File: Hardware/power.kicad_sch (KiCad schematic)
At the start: 42 parts, among them IC1 LTC4413EDD#PBF, J3 XT30PW-M, Q1 SISS23DN-T1-GE3, Q5 SSM3K15AMFV,L3F, U3 LM66200DRLR, U4 MAX77827AEFD+T, U5 SC4215ASTRT

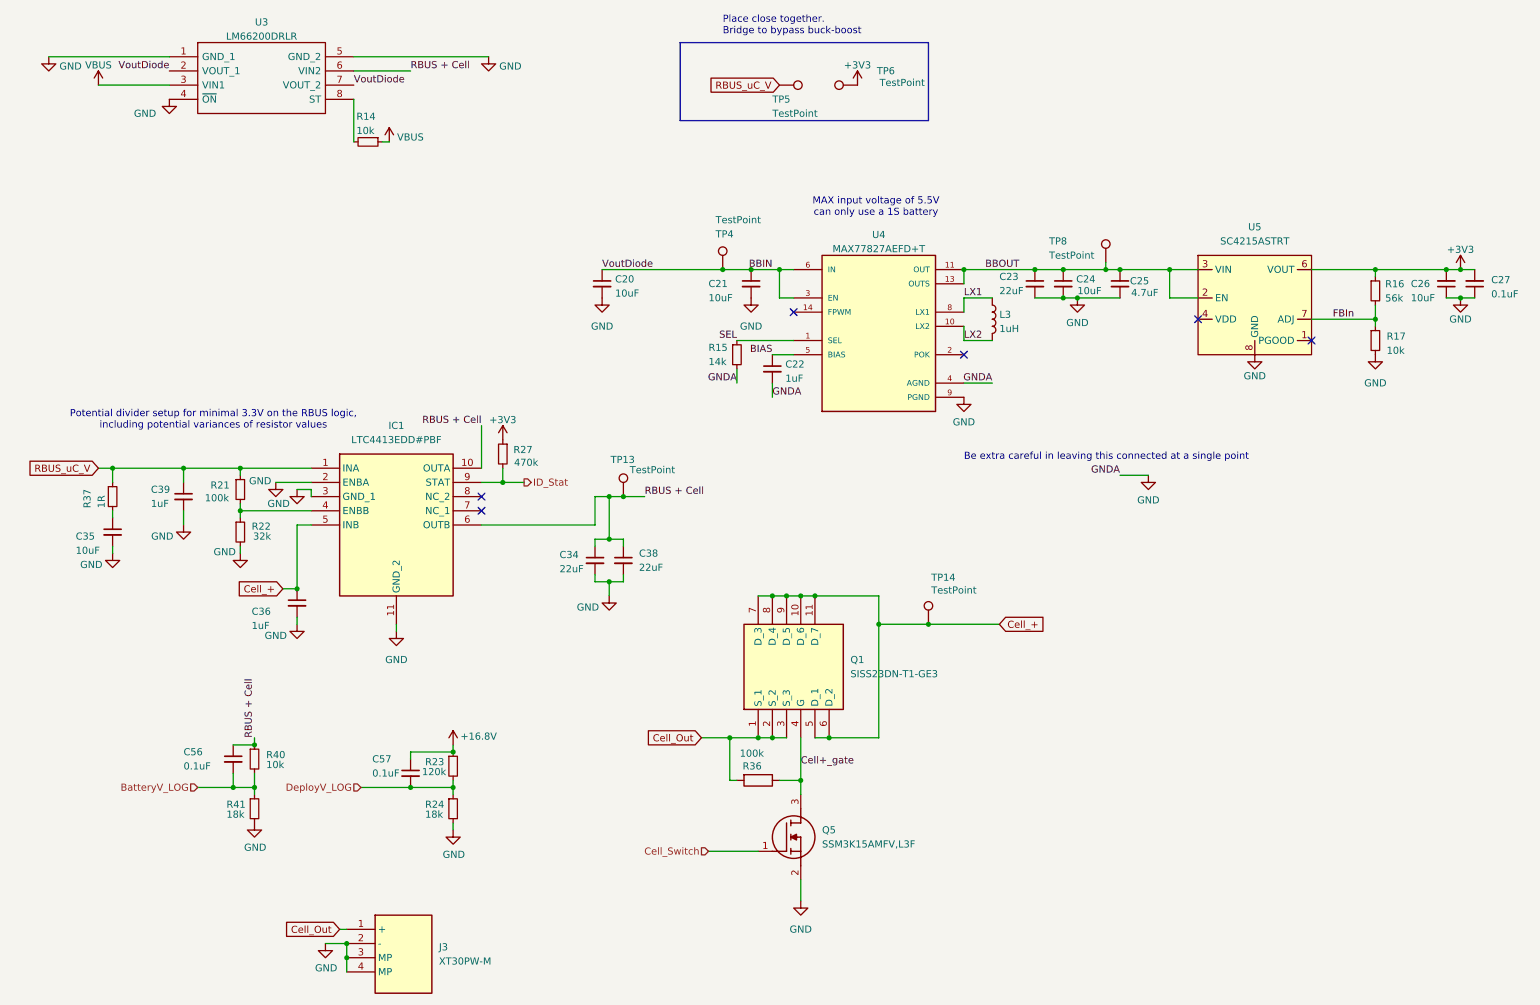
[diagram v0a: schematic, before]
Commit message: More V2 changes
Mainly changed to use Ω symbol for resistors. Fixed the CDC pin for the buck boost
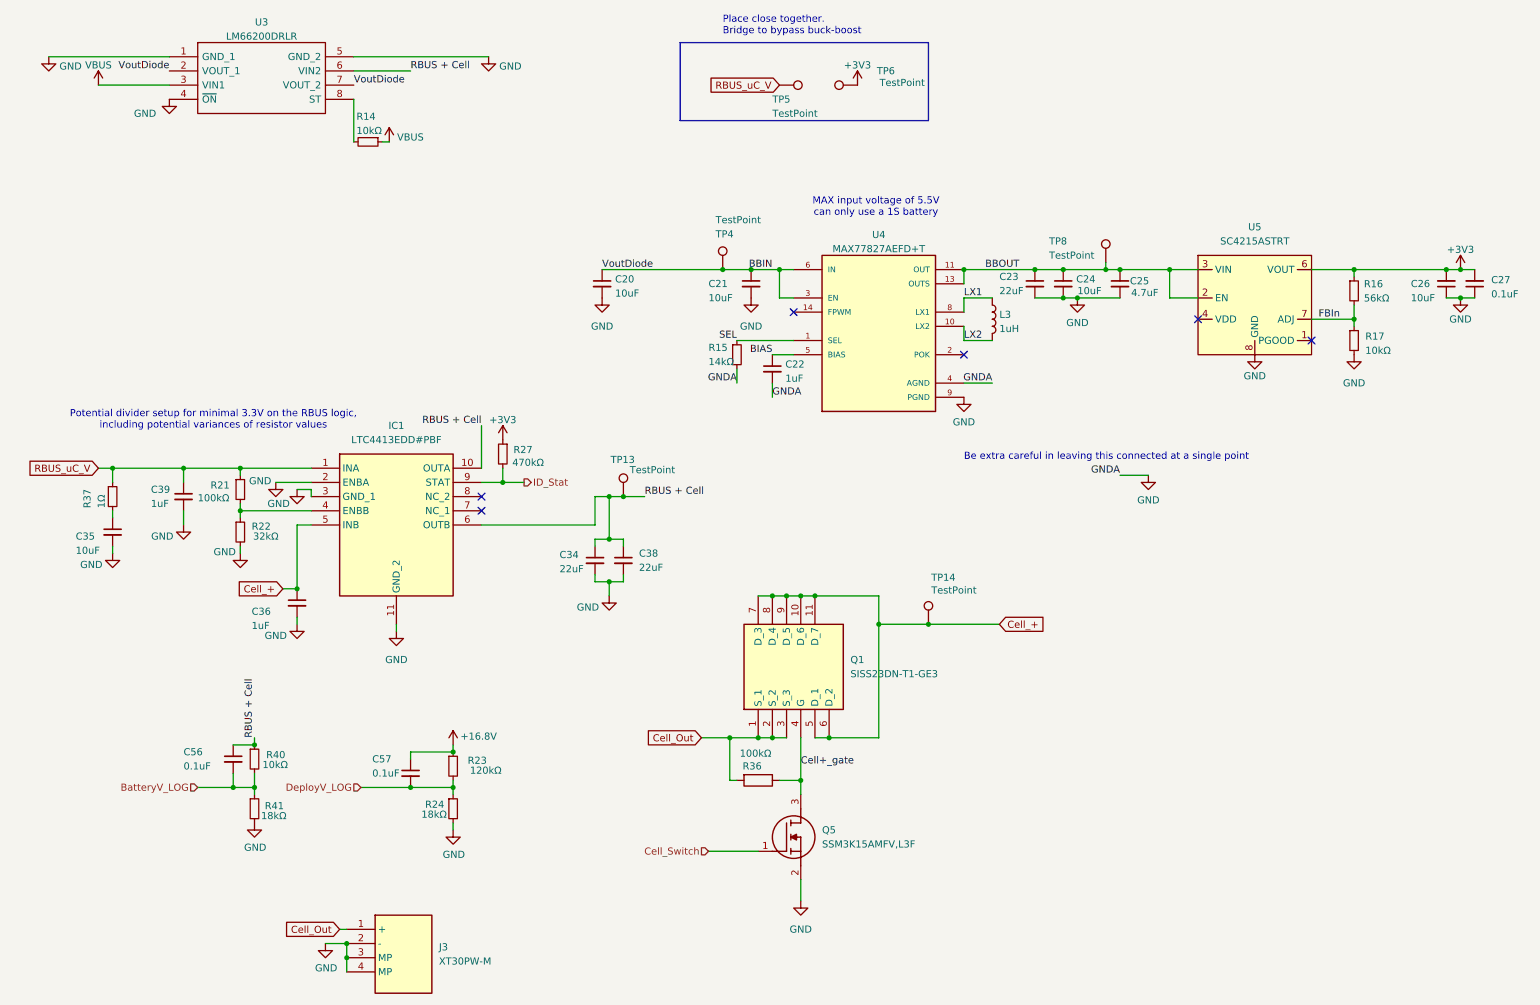
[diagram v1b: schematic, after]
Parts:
- R14, R17, R40: value 10k -> 10kΩ
- R15: value 14k -> 14kΩ
- R16: value 56k -> 56kΩ
- R21, R36: value 100k -> 100kΩ
- R22: value 32k -> 32kΩ
- R23: value 120k -> 120kΩ
- R24, R41: value 18k -> 18kΩ
- R27: value 470k -> 470kΩ
- R37: value 1R -> 1Ω
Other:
- moved on the sheet: R16, R17
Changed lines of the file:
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@@
 	)
 	(junction
-		(at 254 62.23)
+		(at 269.24 62.23)
 		(diameter 0)
 		(color 0 0 0 0)
 	)
 	(junction
-		(at 269.24 62.23)
+		(at 97.79 100.33)
 		(diameter 0)
 		(color 0 0 0 0)
 	)
 	(junction
-		(at 97.79 100.33)
+		(at 250.19 62.23)
 		(diameter 0)
 		(color 0 0 0 0)
@@
 	)
 	(junction
+		(at 250.19 71.12)
+		(diameter 0)
+		(color 0 0 0 0)
+	)
+	(junction
 		(at 69.85 185.42)
 		(diameter 0)
@@
 	)
 	(junction
-		(at 254 71.12)
-		(diameter 0)
-		(color 0 0 0 0)
-	)
-	(junction
 		(at 119.38 102.87)
 		(diameter 0)
@@
 	(wire
 		(pts
-			(xy 254 62.23) (xy 254 63.5)
+			(xy 250.19 62.23) (xy 250.19 63.5)
 		)
 		(stroke
@@
 	(wire
 		(pts
-			(xy 242.57 62.23) (xy 254 62.23)
+			(xy 242.57 62.23) (xy 250.19 62.23)
 		)
 		(stroke
@@
 	(wire
 		(pts
-			(xy 254 68.58) (xy 254 71.12)
+			(xy 250.19 68.58) (xy 250.19 71.12)
 		)
 		(stroke
@@
 	(wire
 		(pts
-			(xy 242.57 71.12) (xy 254 71.12)
+			(xy 242.57 71.12) (xy 250.19 71.12)
 		)
 		(stroke
@@
 	(wire
 		(pts
+			(xy 250.19 62.23) (xy 266.7 62.23)
+		)
+		(stroke
+			(width 0)
+			(type default)
+		)
+	)
+	(wire
+		(pts
 			(xy 81.28 26.67) (xy 71.12 26.67)
 		)
@@
 	(wire
 		(pts
-			(xy 254 71.12) (xy 254 72.39)
+			(xy 250.19 71.12) (xy 250.19 72.39)
 		)
 		(stroke
@@
 	(wire
 		(pts
-			(xy 254 62.23) (xy 266.7 62.23)
-		)
-		(stroke
-			(width 0)
-			(type default)
-		)
-	)
-	(wire
-		(pts
 			(xy 63.5 101.6) (xy 63.5 102.87)
 		)
@@
 	)
 	(label "FBIn"
-		(at 250.19 71.12 180)
+		(at 247.65 71.12 180)
 		(effects
 			(font
@@
 			)
 		)
-		(property "Value" "14k"
+		(property "Value" "14kΩ"
 			(at 134.62 78.7369 0)
 			(effects
@@
 			)
 		)
-		(property "Value" "100k"
+		(property "Value" "100kΩ"
 			(at 140.208 148.844 90)
 			(effects
@@
 		(dnp no)
 		(property "Reference" "R41"
-			(at 50.038 157.988 0)
+			(at 56.896 158.242 0)
 			(effects
 				(font
@@
 			)
 		)
-		(property "Value" "18k"
-			(at 49.9364 159.766 0)
+		(property "Value" "18kΩ"
+			(at 56.7944 160.02 0)
 			(effects
 				(font
@@
 			)
 		)
-		(property "Value" "10k"
+		(property "Value" "10kΩ"
 			(at 71.5911 37.3679 90)
 			(effects
@@
 	(symbol
 		(lib_id "Device:R_Small")
-		(at 254 74.93 0)
+		(at 250.19 74.93 0)
 		(unit 1)
 		(exclude_from_sim no)
@@
 		(dnp no)
 		(property "Reference" "R17"
-			(at 256.014 74.1797 0)
+			(at 252.204 74.1797 0)
 			(effects
 				(font
@@
 			)
 		)
-		(property "Value" "10k"
-			(at 256.014 76.7197 0)
+		(property "Value" "10kΩ"
+			(at 252.204 76.7197 0)
 			(effects
 				(font
@@
 		)
 		(property "Footprint" "Resistor_SMD:R_0402_1005Metric"
-			(at 254 74.93 0)
+			(at 250.19 74.93 0)
 			(effects
 				(font
@@
 		)
 		(property "Datasheet" "~"
-			(at 254 74.93 0)
+			(at 250.19 74.93 0)
 			(effects
 				(font
@@
 		)
 		(property "Description" ""
-			(at 254 74.93 0)
+			(at 250.19 74.93 0)
 			(effects
 				(font
@@
 			)
 		)
-		(property "Value" "470k"
-			(at 104.14 96.774 0)
+		(property "Value" "470kΩ"
+			(at 105.156 96.774 0)
 			(effects
 				(font
@@
 			)
 		)
-		(property "Value" "10k"
+		(property "Value" "10kΩ"
 			(at 57.0484 150.876 0)
 			(effects
@@
 			)
 		)
-		(property "Value" "32k"
+		(property "Value" "32kΩ"
 			(at 53.086 109.982 0)
 			(effects
@@
 		(dnp no)
 		(property "Reference" "R23"
-			(at 85.598 150.368 0)
+			(at 93.218 150.114 0)
 			(effects
 				(font
@@
 			)
 		)
-		(property "Value" "120k"
-			(at 85.4964 152.146 0)
+		(property "Value" "120kΩ"
+			(at 94.742 151.892 0)
 			(effects
 				(font
@@
 			)
 		)
-		(property "Value" "1R"
+		(property "Value" "1Ω"
 			(at 25.9379 104.9389 90)
 			(effects
@@
 			)
 		)
-		(property "Value" "18k"
+		(property "Value" "18kΩ"
 			(at 85.4964 159.766 0)
 			(effects
@@
 			)
 		)
-		(property "Value" "100k"
-			(at 44.45 103.124 0)
+		(property "Value" "100kΩ"
+			(at 43.18 103.124 0)
 			(effects
 				(font
@@
 	(symbol
 		(lib_id "power:GND")
-		(at 254 77.47 0)
+		(at 250.19 77.47 0)
 		(unit 1)
 		(exclude_from_sim no)
@@
 		(fields_autoplaced yes)
 		(property "Reference" "#PWR048"
-			(at 254 83.82 0)
+			(at 250.19 83.82 0)
 			(effects
 				(font
@@
 		)
 		(property "Value" "GND"
-			(at 254 82.55 0)
+			(at 250.19 82.55 0)
 			(effects
 				(font
@@
 		)
 		(property "Footprint" ""
-			(at 254 77.47 0)
+			(at 250.19 77.47 0)
 			(effects
 				(font
@@
 		)
 		(property "Datasheet" ""
-			(at 254 77.47 0)
+			(at 250.19 77.47 0)
 			(effects
 				(font
@@
 		)
 		(property "Description" ""
-			(at 254 77.47 0)
+			(at 250.19 77.47 0)
 			(effects
 				(font
@@
 	(symbol
 		(lib_id "Device:R_Small")
-		(at 254 66.04 0)
+		(at 250.19 66.04 0)
 		(unit 1)
 		(exclude_from_sim no)
@@
 		(dnp no)
 		(property "Reference" "R16"
-			(at 255.7567 64.8105 0)
+			(at 251.9467 64.8105 0)
 			(effects
 				(font
@@
 			)
 		)
-		(property "Value" "56k"
-			(at 255.7567 67.3505 0)
+		(property "Value" "56kΩ"
+			(at 251.9467 67.3505 0)
 			(effects
 				(font
@@
 		)
 		(property "Footprint" "Resistor_SMD:R_0402_1005Metric"
-			(at 254 66.04 0)
+			(at 250.19 66.04 0)
 			(effects
 				(font
@@
 		)
 		(property "Datasheet" "~"
-			(at 254 66.04 0)
+			(at 250.19 66.04 0)
 			(effects
 				(font
@@
 		)
 		(property "Description" ""
-			(at 254 66.04 0)
+			(at 250.19 66.04 0)
 			(effects
 				(font

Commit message: reformatted and renamed file
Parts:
- C203: renamed from C56; value 0.1uF -> 100nF
- C205: renamed from C57; value 0.1uF -> 100nF
- C215: renamed from C27; value 0.1uF -> 100nF
- TP201: renamed from TP13; now left out of the parts list
- TP202: renamed from TP4; now left out of the parts list
- TP203: renamed from TP5; now left out of the parts list
- TP204: renamed from TP6; now left out of the parts list
- TP205: renamed from TP14; now left out of the parts list
- TP206: renamed from TP8; now left out of the parts list
- renumbered C35 to C201, C39 to C202, C36 to C204, C34 to C206, C20 to C207, C38 to C208, C21 to C209, C22 to C210, C23 to C211, C24 to C212, C25 to C213, C26 to C214, J3 to J201, L3 to L201, Q1 to Q201, Q5 to Q202, R37 to R201, R21 to R202, R22 to R203, R40 to R204, R41 to R205, R14 to R206, R23 to R207, R24 to R208, R27 to R209, R15 to R210, R36 to R211, R16 to R212, R17 to R213, U3 to U201, IC1 to U202, U4 to U203, U5 to U204

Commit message: changed 1 footprint
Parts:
- Q202: footprint iclr:SSM3K15AMFVL3F -> Package_TO_SOT_SMD:SOT-723
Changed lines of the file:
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@@
 			)
 		)
-		(property "Footprint" "iclr:SSM3K15AMFVL3F"
+		(property "Footprint" "Package_TO_SOT_SMD:SOT-723"
 			(at 154.94 265.1 0)
 			(effects
